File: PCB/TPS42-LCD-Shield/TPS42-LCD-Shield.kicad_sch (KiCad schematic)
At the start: 31 parts, among them J4 PJ-320A, J5 Conn_01x06, J6 OLED, J7 FH12-10S-0.5SH, J8 Conn_01x06

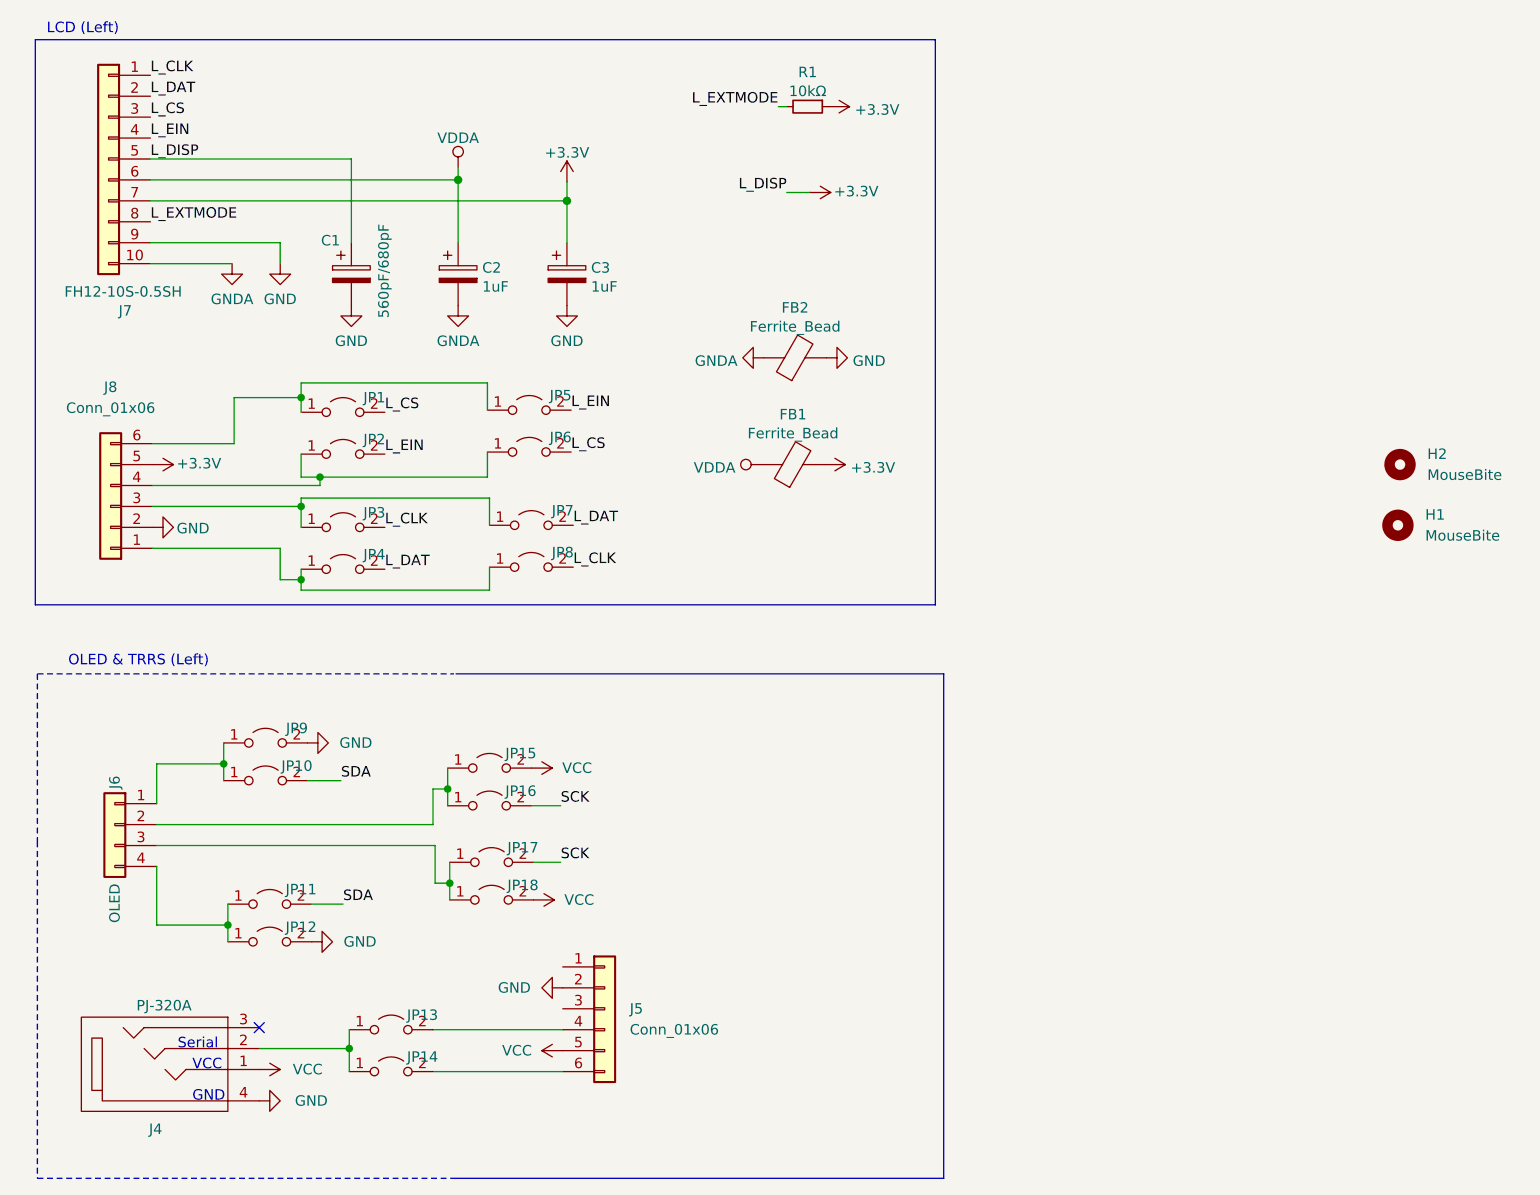
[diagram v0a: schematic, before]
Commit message: splitted shields
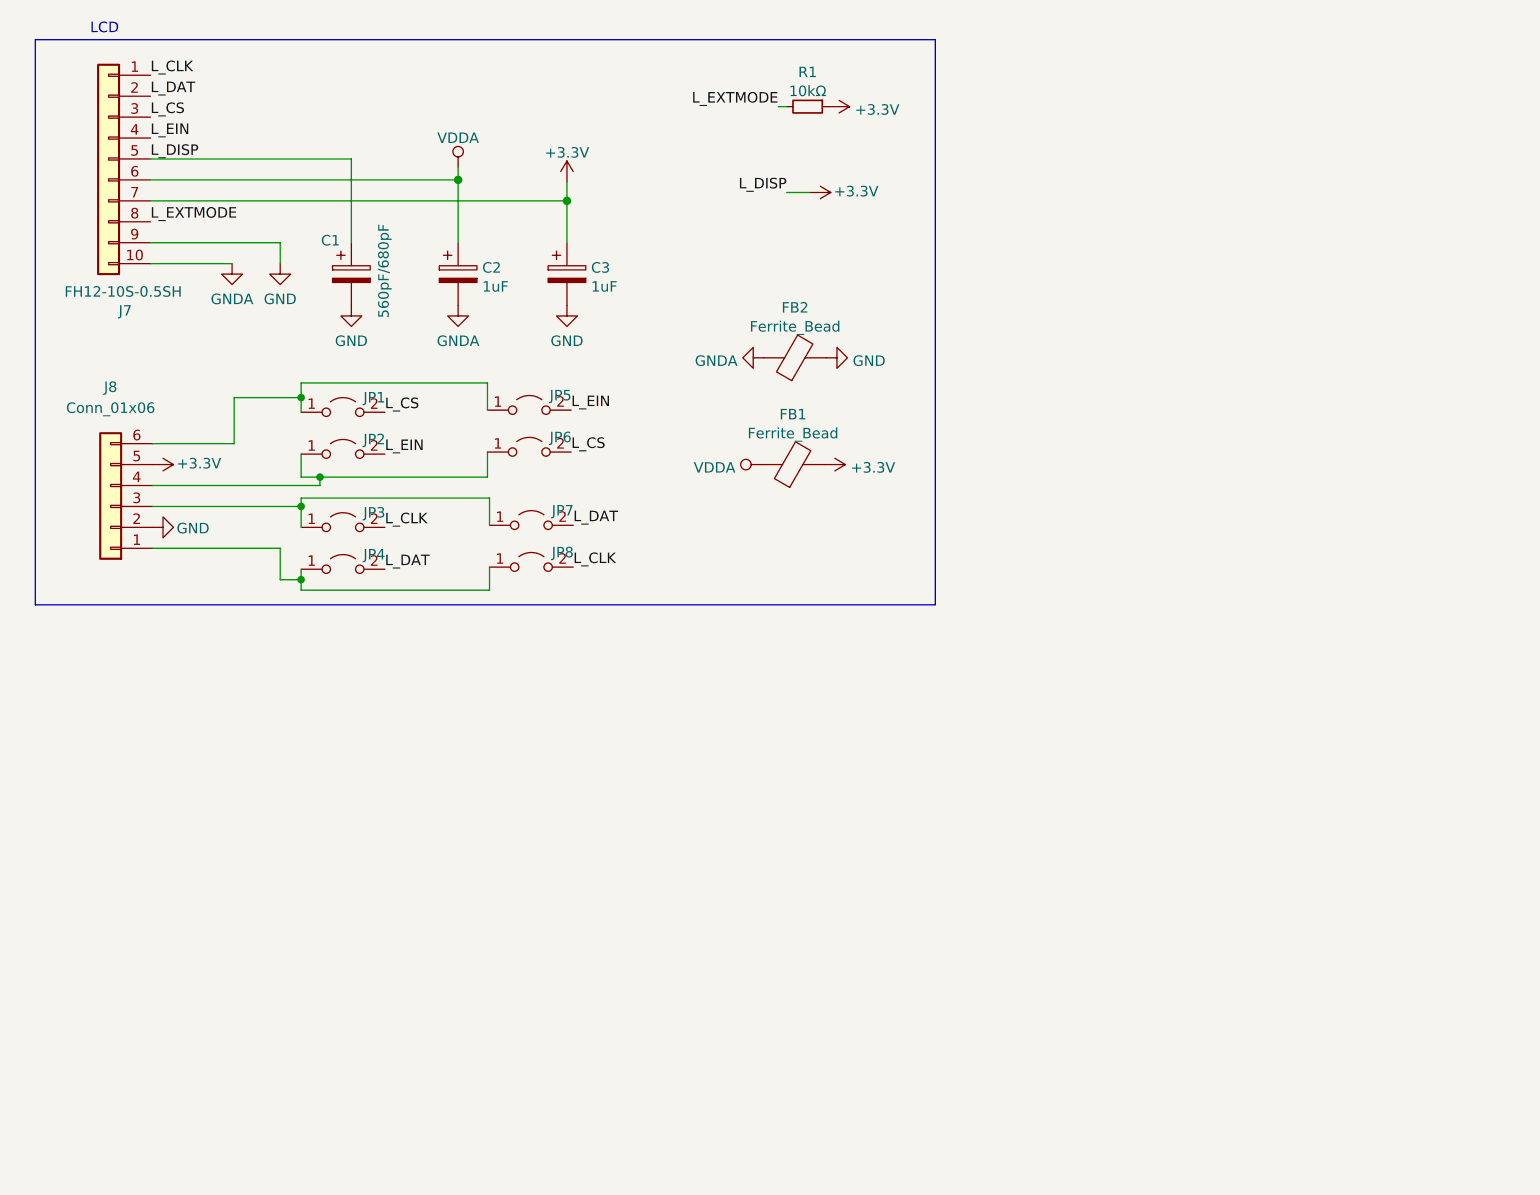
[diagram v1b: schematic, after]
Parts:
- removed H1, H2: MouseBite, TPS42-Shield:mouse-bite-2mm-slot, symbol Mechanical:MountingHole
- removed J4: PJ-320A, TPS42-Shield:MJ-4PP-9-reversable, symbol TPS42:MJ-4PP-9
- removed J5: Conn_01x06, Connector_PinHeader_2.54mm:PinHeader_2x03_P2.54mm_Vertical, symbol Connector_Generic:Conn_01x06
- removed J6: OLED, TPS42-Shield:OLED, symbol Connector_Generic:Conn_01x04
- removed JP10, JP11, JP12, JP13, JP14, JP15, JP16, JP17, JP18, JP9: Jumper_2_Open, Jumper:SolderJumper-2_P1.3mm_Open_TrianglePad1.0x1.5mm, symbol Jumper:Jumper_2_Open
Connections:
- no-connect marks 1 -> 0
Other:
- note added: "LCD"
- note removed: "GND"
- note removed: "LCD (Left)"
- note removed: "OLED & TRRS (Left)"
- note removed: "Serial"
- note removed: "VCC"

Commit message: finalizing
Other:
- title: (none) -> TPS42 LCD Shield
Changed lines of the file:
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@@
 (kicad_sch (version 20211123) (generator eeschema)
   (paper "A4")
+  (title_block
+    (title "TPS42 LCD Shield")
+    (date "2022-05-19")
+    (rev "${Revision}")
+  )
   (junction (at 49.784 83.566) (diameter 0) (color 0 0 0 0)
   )
